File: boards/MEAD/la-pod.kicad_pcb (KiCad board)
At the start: 4 copper layers, 177 parts, among them J1 CONN_SFF8087, J2 PINHEADER_1x5, J3 LSHM-120-02.5-L-DV-A-N-K-TR, J4 AMG240160P-G-W6WFDW, U1 LMH7322, U14 TPS62173, U15 LM27761, U2 LMH7322, U3 LMH7322, U4 LMH7322, U5 STM32F031-QFN28, U6 DAC60508ZRTET, U7 TPS62170, U8 LP5907SNX-3.3/NOPB, U9 TPS62170

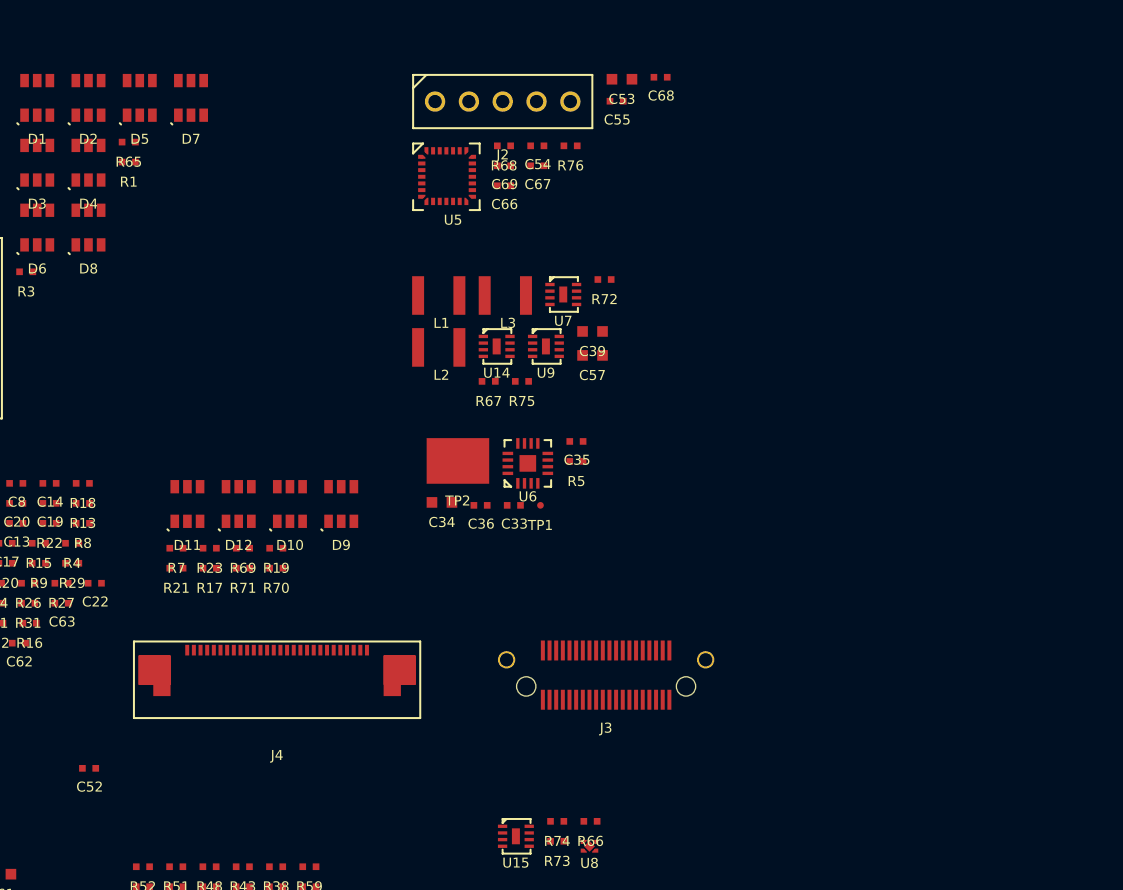
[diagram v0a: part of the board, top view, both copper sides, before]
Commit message: MEAD: finished schematic review, added more test points
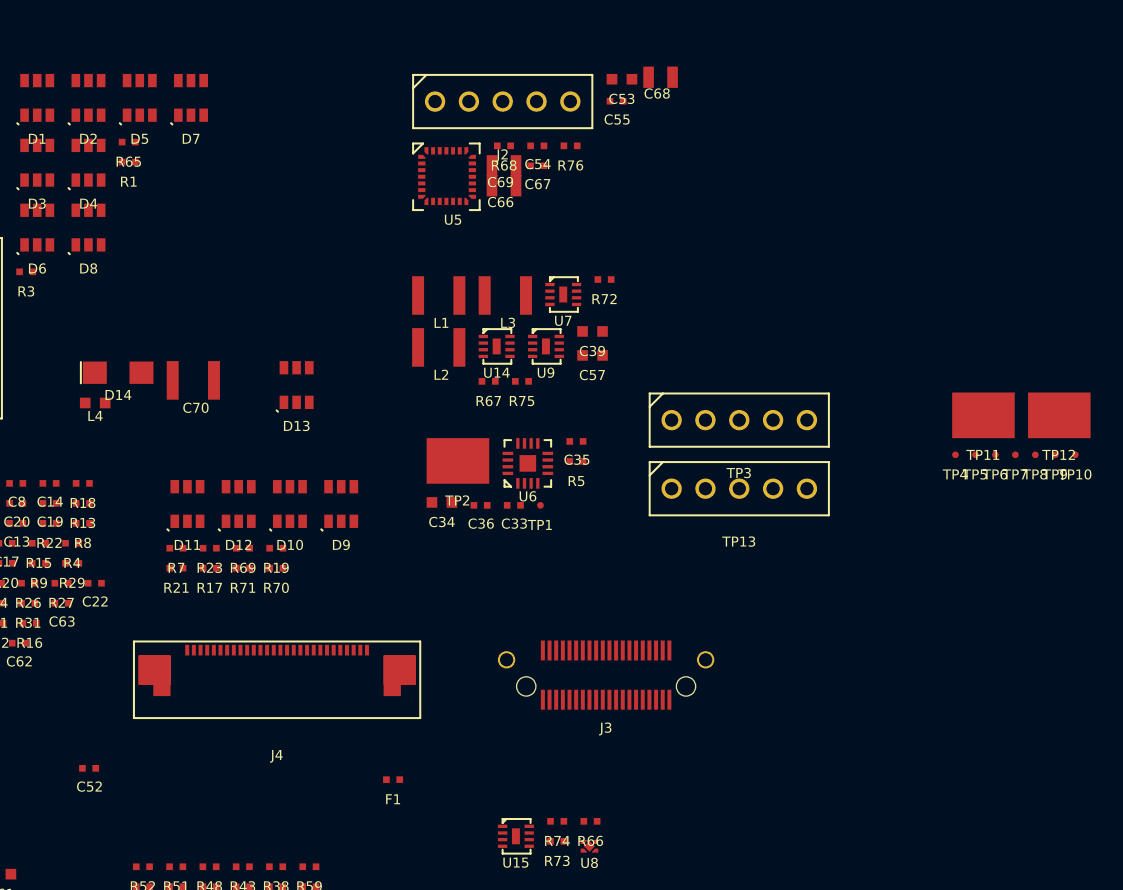
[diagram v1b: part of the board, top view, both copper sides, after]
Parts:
- added C70: 22 uF, azonenberg_pcb:EIA_1210_CAP_NOSILK, F.Cu at (69.0, 48.0)
- added D13: SP4010, azonenberg_pcb:SOT23_6, F.Cu at (76.8, 48.4)
- added D14: SMAJ12A, azonenberg_pcb:SMA, F.Cu at (63.4, 47.4)
- added F1: 1A, azonenberg_pcb:EIA_0402_RES_NOSILK, F.Cu at (84.0, 78.0)
- added L4: 600R, azonenberg_pcb:EIA_0603_INDUCTOR_NOSILK, F.Cu at (61.6, 49.7)
- added TP10: TESTPAD, azonenberg_pcb:TESTPOINT_SMT_0.5MM, F.Cu at (135.2, 53.6)
- added TP11: TESTCLIP, azonenberg_pcb:TESTPOINT_SMT_KEYSTONE_5016, F.Cu at (128.3, 50.6)
- added TP12: TESTCLIP, azonenberg_pcb:TESTPOINT_SMT_KEYSTONE_5016, F.Cu at (134.0, 50.6)
- added TP13: PINHEADER_1x5, azonenberg_pcb:CONN_HEADER_2.54MM_1x5, F.Cu at (110.0, 56.1)
- added TP3: PINHEADER_1x5, azonenberg_pcb:CONN_HEADER_2.54MM_1x5, F.Cu at (110.0, 51.0)
- added TP4: TESTPAD, azonenberg_pcb:TESTPOINT_SMT_0.5MM, F.Cu at (126.2, 53.6)
- added TP5: TESTPAD, azonenberg_pcb:TESTPOINT_SMT_0.5MM, F.Cu at (127.7, 53.6)
- added TP6: TESTPAD, azonenberg_pcb:TESTPOINT_SMT_0.5MM, F.Cu at (129.2, 53.6)
- added TP7: TESTPAD, azonenberg_pcb:TESTPOINT_SMT_0.5MM, F.Cu at (130.7, 53.6)
- added TP8: TESTPAD, azonenberg_pcb:TESTPOINT_SMT_0.5MM, F.Cu at (132.2, 53.6)
- added TP9: TESTPAD, azonenberg_pcb:TESTPOINT_SMT_0.5MM, F.Cu at (133.7, 53.6)
- C66, C68, C69: footprint azonenberg_pcb:EIA_0402_CAP_NOSILK -> azonenberg_pcb:EIA_0805_CAP_NOSILK
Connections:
- net /Comparators/VREF0 renamed /VREF0
- C37 pad 1: /12V0 -> Net-(C37-Pad1)
- C40 pad 1: /12V0 -> Net-(C37-Pad1)
- C61 pad 1: /1V5_N -> Net-(C61-Pad1)
- U15 pad 4: /1V5_N -> Net-(C61-Pad1)
- U7 pad 2: /12V0 -> Net-(C37-Pad1)

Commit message: Continued MEAD layout
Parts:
- C1, C13, C17, C21, C25, C29, C44, C48, C5, C62, C67, C9, F1, R2, R33, R34, R35, R36, R4, R49, R50, R51, R52, R76: moved to B.Cu
- moved TP3 87.4 mm to (25.3, 29.3), turned to 90 degrees
- moved TP13 84.0 mm to (30.4, 29.3), turned to 90 degrees
- moved D6 79.4 mm to (123.9, 79.7)
- moved C59 78.2 mm to (98.5, 38.4), turned to 90 degrees
- moved D5 76.6 mm to (119.9, 80.2)
- moved TP10 74.7 mm to (63.3, 73.9)
- moved C23 73.5 mm to (116.8, 86.1)
- moved C47 72.4 mm to (112.8, 86.1)
- moved C28 71.4 mm to (123.7, 66.9)
- moved C43 71.1 mm to (99.0, 24.9), turned to 90 degrees
- moved C37 69.9 mm to (82.5, 25.5), turned to 180 degrees
- moved C38 69.9 mm to (84.0, 31.7), turned to 180 degrees
- moved C56 69.8 mm to (88.6, 30.0), turned to 90 degrees
- moved C60 69.3 mm to (99.1, 31.3), turned to 90 degrees
- moved C40 68.8 mm to (88.6, 23.5), turned to 90 degrees
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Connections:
- C37 pad 1: Net-(C37-Pad1) -> /Power Supply/12V0_FUSED
- C40 pad 1: Net-(C37-Pad1) -> /Power Supply/12V0_FUSED
- C42 pad 1: /12V0 -> /Power Supply/12V0_FUSED
- C56 pad 1: /12V0 -> /Power Supply/12V0_FUSED
- D14 pad 1: /12V0 -> /Power Supply/12V0_FUSED
- D2 pad 1: /TX1_P -> /TX1_N
- D2 pad 3: /TX1_N -> /TX1_P
- F1 pad 1: Net-(C37-Pad1) -> /Power Supply/12V0_FUSED
- J1 pad B2: /TX0_P -> /TX0_N
- J1 pad B3: /TX0_N -> /TX0_P
- R11 pad 1: /Comparators/1V0_N -> /1V5_N
- R13 pad 1: /Comparators/1V0_N -> /1V5_N
- R15 pad 1: /Comparators/1V0_N -> /1V5_N
- R25 pad 1: /Comparators/1V0_N -> /1V5_N
- R27 pad 1: /Comparators/1V0_N -> /1V5_N
- R29 pad 1: /Comparators/1V0_N -> /1V5_N
- R31 pad 1: /Comparators/1V0_N -> /1V5_N
- R9 pad 1: /Comparators/1V0_N -> /1V5_N
- TP12 pad 1: (no net) -> /GND
- TP4 pad 1: /12V0 -> /Power Supply/12V0_FUSED
- U1 pad 11: /Comparators/CH1 -> /Comparators/CH0
- U1 pad 12: /Comparators/VREF1 -> /VREF0
- U1 pad 19: /TX1_N -> /TX0_N
- U1 pad 20: /TX1_P -> /TX0_P
- U1 pad 23: /TX0_P -> /TX1_P
- U1 pad 24: /TX0_N -> /TX1_N
- U1 pad 7: /VREF0 -> /Comparators/VREF1
- U1 pad 8: /Comparators/CH0 -> /Comparators/CH1
- U14 pad 2: /12V0 -> /Power Supply/12V0_FUSED
- U14 pad 3: /12V0 -> /Power Supply/12V0_FUSED
- U7 pad 2: Net-(C37-Pad1) -> /Power Supply/12V0_FUSED
- U7 pad 3: /12V0 -> /Power Supply/12V0_FUSED
- U9 pad 2: /12V0 -> /Power Supply/12V0_FUSED
- U9 pad 3: /12V0 -> /Power Supply/12V0_FUSED
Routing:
- net /GND: track 0.00 -> 529.7 mm, vias 0 -> 224
- net /Power Supply/12V0_FUSED: track 0.00 -> 86.4 mm, vias 0 -> 23
- net /2V5: track 0.00 -> 73.9 mm, vias 0 -> 23
- net /5V0: track 0.00 -> 71.0 mm, vias 0 -> 13
- net /6V0: track 0.00 -> 61.3 mm, vias 0 -> 12
- net /3V3: track 0.00 -> 52.9 mm, vias 0 -> 4
- net /1V5_N: track 0.00 -> 47.8 mm, vias 0 -> 12
- net /TX0_P: track 0.00 -> 31.7 mm, vias 0 -> 2
- net /TX0_N: track 0.00 -> 31.7 mm, vias 0 -> 2
- net /TX1_N: track 0.00 -> 29.4 mm, vias 0 -> 2
- net /TX1_P: track 0.00 -> 29.3 mm, vias 0 -> 2
- net /TX5_N: track 0.00 -> 17.8 mm, vias 0 -> 1
- net /TX5_P: track 0.00 -> 17.2 mm, vias 0 -> 1
- net /TX4_N: track 0.00 -> 15.4 mm, vias 0 -> 1
- net /TX4_P: track 0.00 -> 14.8 mm, vias 0 -> 1
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- added copper zone on F.Cu, net /GND

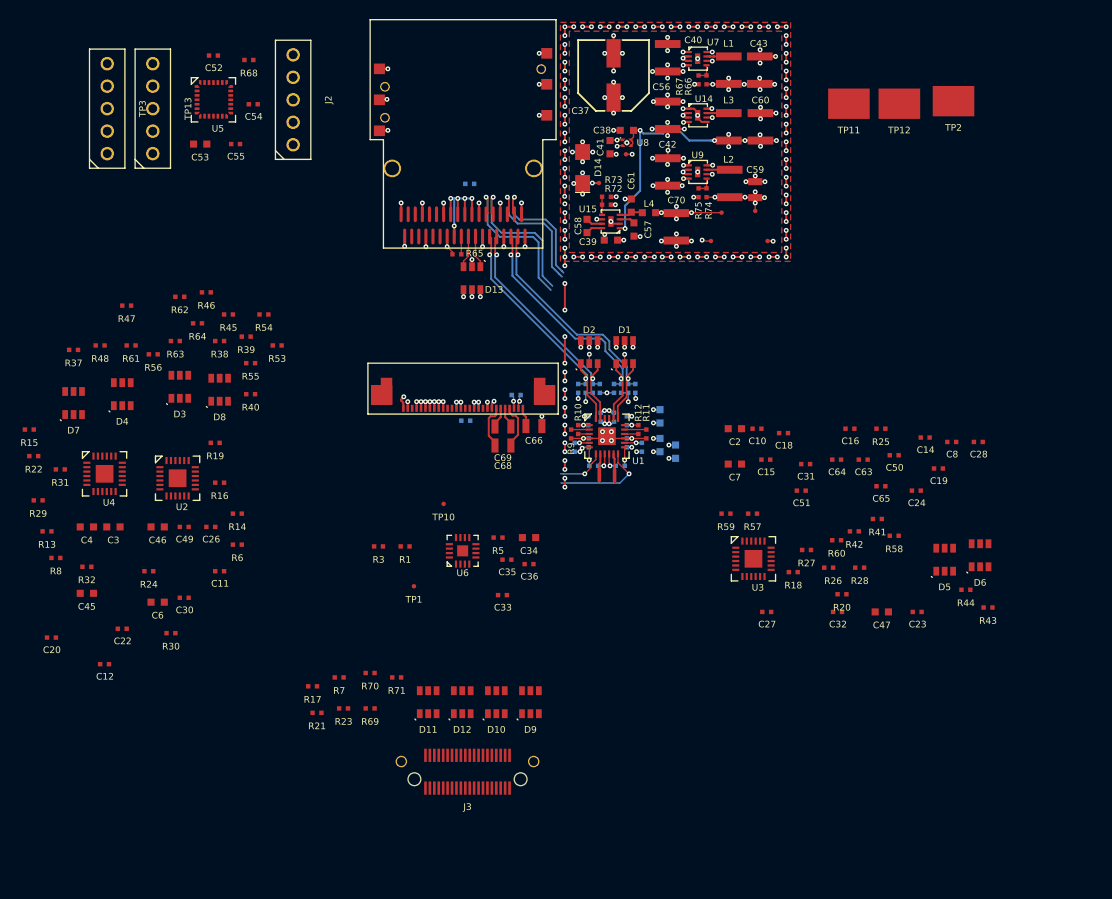
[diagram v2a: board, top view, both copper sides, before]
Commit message: Continued MEAD layout. Right side is almost done.
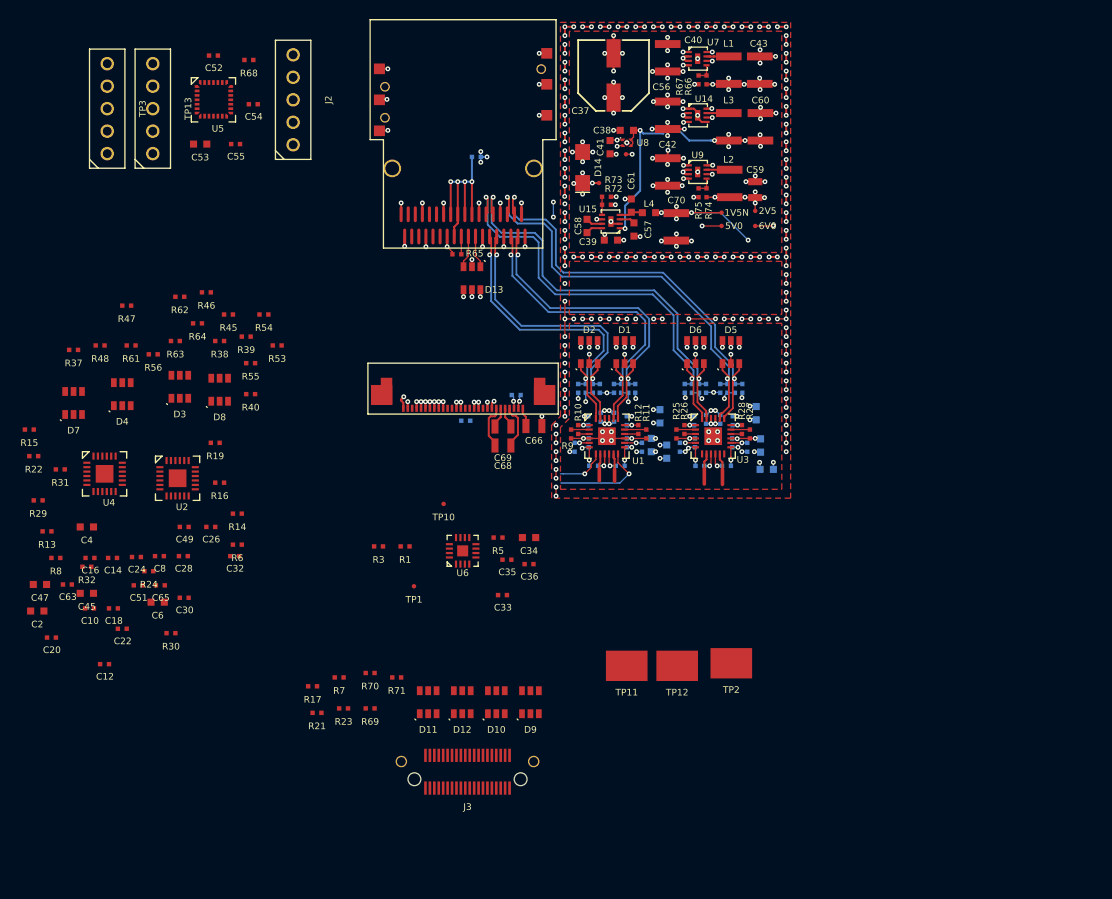
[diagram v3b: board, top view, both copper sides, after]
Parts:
- C11, C15, C19, C23, C27, C3, C31, C46, C50, C64, C7, R18, R20, R41, R42, R43, R44, R57, R58, R59, R60: moved to B.Cu
- moved C47 95.2 mm to (17.7, 83.0)
- moved C14 92.8 mm to (25.9, 80.0)
- moved C63 91.0 mm to (20.8, 83.0)
- moved C28 90.7 mm to (33.9, 79.8)
- moved C8 90.4 mm to (31.2, 79.8)
- moved C24 88.4 mm to (28.6, 79.9)
- moved C16 87.1 mm to (23.4, 80.0)
- moved C65 82.2 mm to (31.3, 83.1)
- moved C2 81.4 mm to (17.4, 86.0)
- moved C18 78.2 mm to (26.0, 85.7)
- moved C10 78.1 mm to (23.3, 85.7)
- moved C51 75.7 mm to (28.8, 83.1)
- moved C3 74.1 mm to (99.8, 70.0)
- moved C46 68.7 mm to (99.1, 67.3), turned to 270 degrees
- moved C32 68.4 mm to (39.7, 79.8)
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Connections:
- D13 pad 4: /2V5 -> /3V3
- D13 pad 5: /2V5 -> /3V3
- D13 pad 6: /2V5 -> /3V3
- D6 pad 1: /TX5_P -> /TX5_N
- D6 pad 3: /TX5_N -> /TX5_P
- J1 pad A2: /TX4_P -> /TX4_N
- J1 pad A3: /TX4_N -> /TX4_P
- U3 pad 11: /Comparators/CH5 -> /Comparators/CH4
- U3 pad 12: /Comparators/VREF5 -> /Comparators/VREF4
- U3 pad 19: /TX5_N -> /TX4_N
- U3 pad 20: /TX5_P -> /TX4_P
- U3 pad 23: /TX4_P -> /TX5_P
- U3 pad 24: /TX4_N -> /TX5_N
- U3 pad 7: /Comparators/VREF4 -> /Comparators/VREF5
- U3 pad 8: /Comparators/CH4 -> /Comparators/CH5
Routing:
- net /GND: track 529.7 -> 624.8 mm, vias 224 -> 284
- net /2V5: track 73.9 -> 138.9 mm, vias 23 -> 34
- net /1V5_N: track 47.8 -> 94.2 mm, vias 12 -> 20
- net /6V0: track 61.3 -> 98.6 mm, vias 12 -> 15
- net /TX4_P: track 14.8 -> 49.9 mm, vias 1 -> 2
- net /TX4_N: track 15.4 -> 49.9 mm, vias 1 -> 2
- net /TX5_P: track 17.2 -> 49.5 mm, vias 1 -> 2
- net /TX5_N: track 17.8 -> 49.5 mm, vias 1 -> 2
- net /5V0: track 71.0 -> 102.0 mm, vias 13 -> 14
- net /Power Supply/12V0_FUSED: track 86.4 -> 101.2 mm, vias 23 -> 26
- net /3V3: track 52.9 -> 66.0 mm, vias 4 -> 7
- net /12V0: track 13.9 -> 22.6 mm, vias 5 -> 4
- net /TX1_P: track 29.3 -> 36.1 mm
- net /TX1_N: track 29.4 -> 36.1 mm
- net /TX0_N: track 31.7 -> 37.9 mm
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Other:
- board text added: "1V5N"
- board text added: "2V5"
- board text added: "5V0"
- board text added: "6V0"

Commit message: Finished MCU layout, began left side comparator layout.
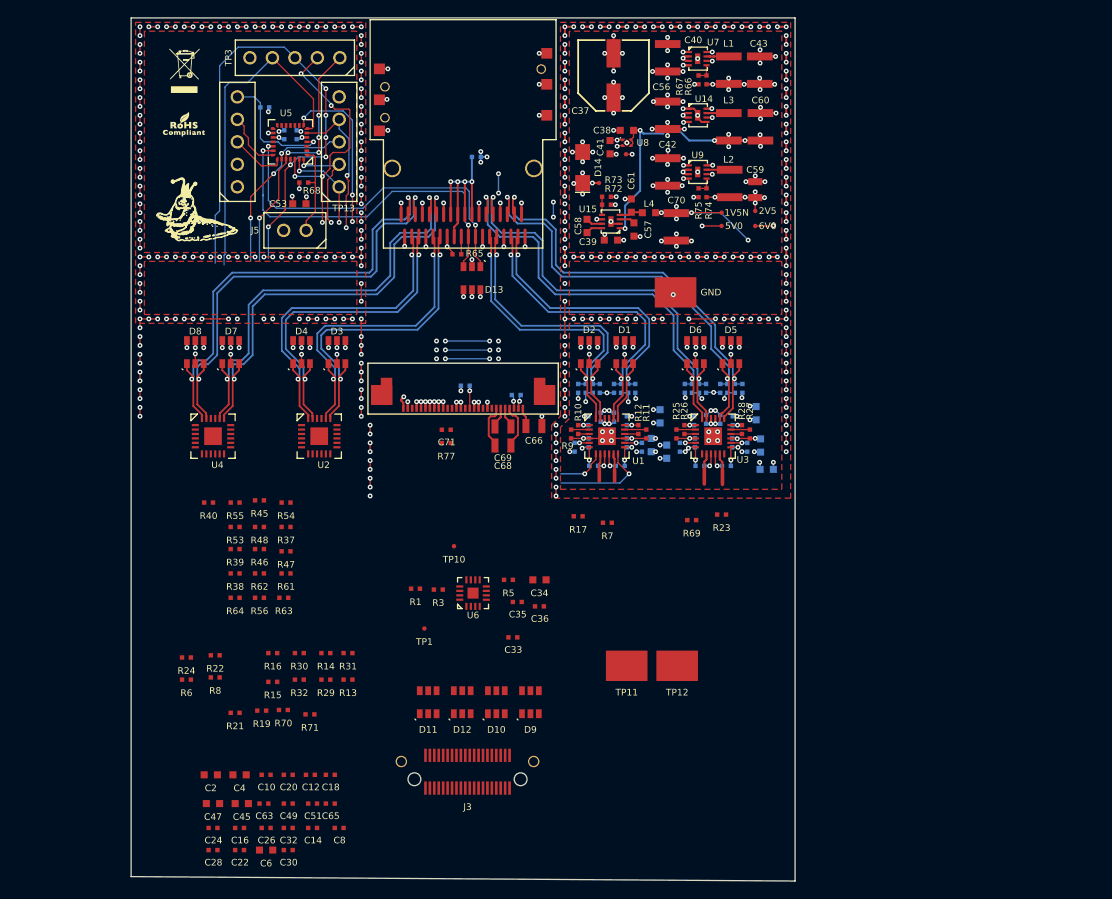
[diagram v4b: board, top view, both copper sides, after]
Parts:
- added C71: 0.47 uF, azonenberg_pcb:EIA_0402_CAP_NOSILK, F.Cu at (63.6, 65.5)
- added G***: LOGO, w_logo:Logo_silk_WEEE_3.4x5mm, F.Cu at (34.0, 25.0)
- added G***: LOGO, w_logo:Logo_silk_ROHS_5x2.8mm, F.Cu at (34.0, 31.0)
- added G***: LOGO, azonenberg_pcb:LONGTHING-1200DPI, F.Cu at (36.0, 41.0)
- added J5: PINHEADER_1x2, azonenberg_pcb:CONN_HEADER_2.54MM_1x2, F.Cu at (46.5, 43.0)
- added R77: 0, azonenberg_pcb:EIA_0402_RES_NOSILK, F.Cu at (63.6, 67.0)
- C52, C54, C55: moved to B.Cu
- moved R23 48.0 mm to (94.7, 75.1)
- moved TP2 42.4 mm to (89.5, 50.0)
- moved R69 42.1 mm to (91.3, 75.7)
- moved R15 39.6 mm to (44.0, 94.0)
- moved R31 38.6 mm to (52.5, 90.8)
- moved R29 38.3 mm to (50.0, 93.8)
- moved C14 38.0 mm to (48.5, 110.5)
- moved R13 37.9 mm to (52.5, 93.8)
- moved C8 36.8 mm to (51.5, 110.5)
- moved R17 35.6 mm to (78.5, 75.3)
- moved R7 35.0 mm to (81.8, 76.0)
- moved C16 34.9 mm to (40.2, 110.5)
- moved C26 34.6 mm to (43.2, 110.5)
- moved C49 33.4 mm to (45.8, 107.8)
- moved C28 33.4 mm to (37.2, 113.0)
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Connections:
- net Net-(R68-Pad1) renamed /MCU/BOOT0
- D4 pad 1: /TX3_P -> /TX3_N
- D4 pad 3: /TX3_N -> /TX3_P
- D8 pad 1: /TX7_P -> /TX7_N
- D8 pad 3: /TX7_N -> /TX7_P
- J1 pad A13: /TX6_P -> /TX6_N
- J1 pad A14: /TX6_N -> /TX6_P
- J1 pad B13: /TX2_P -> /TX2_N
- J1 pad B14: /TX2_N -> /TX2_P
- J4 pad 8: /3V3 -> /MCU/LCD_VDD
- U2 pad 11: /Comparators/CH3 -> /Comparators/CH2
- U2 pad 12: /Comparators/VREF3 -> /Comparators/VREF2
- U2 pad 19: /TX3_N -> /TX2_N
- U2 pad 20: /TX3_P -> /TX2_P
- U2 pad 23: /TX2_P -> /TX3_P
- U2 pad 24: /TX2_N -> /TX3_N
- U2 pad 7: /Comparators/VREF2 -> /Comparators/VREF3
- U2 pad 8: /Comparators/CH2 -> /Comparators/CH3
- U4 pad 11: /Comparators/CH7 -> /Comparators/CH6
- U4 pad 12: /Comparators/VREF7 -> /Comparators/VREF6
- U4 pad 19: /TX7_N -> /TX6_N
- U4 pad 20: /TX7_P -> /TX6_P
- U4 pad 23: /TX6_P -> /TX7_P
- U4 pad 24: /TX6_N -> /TX7_N
- U4 pad 7: /Comparators/VREF6 -> /Comparators/VREF7
- U4 pad 8: /Comparators/CH6 -> /Comparators/CH7
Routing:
- net /GND: track 624.8 -> 873.3 mm, vias 284 -> 455
- net /2V5: track 138.9 -> 215.2 mm, vias 34 -> 58
- net /DAC/DAC_MISO: track 0.00 -> 61.7 mm, vias 0 -> 6
- net /TX7_P: track 0.00 -> 50.9 mm, vias 0 -> 2
- net /TX7_N: track 0.00 -> 50.9 mm, vias 0 -> 2
- net /3V3: track 66.0 -> 116.4 mm, vias 7 -> 12
- net /TX6_P: track 0.00 -> 49.0 mm, vias 0 -> 2
- net /TX6_N: track 0.00 -> 49.0 mm, vias 0 -> 2
- net /MCU/LCD_CTRL_DATA: track 0.00 -> 37.4 mm
- net /TX3_P: track 0.00 -> 37.3 mm, vias 0 -> 2
- net /TX3_N: track 0.00 -> 37.3 mm, vias 0 -> 2
- net /UART_RX: track 3.64 -> 41.0 mm, vias 0 -> 2
- net /UART_TX: track 3.64 -> 39.9 mm, vias 0 -> 2
- net /TX2_P: track 0.00 -> 35.8 mm, vias 0 -> 2
- net /TX2_N: track 0.00 -> 35.8 mm, vias 0 -> 2
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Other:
- board outline added: 75 x 97.5 mm
- board text added: "GND"
